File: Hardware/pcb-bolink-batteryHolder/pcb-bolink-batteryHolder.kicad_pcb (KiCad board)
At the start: 2 copper layers, 37 x 64.5 mm, 8 parts, among them J1 Batt-, J2 Batt+, J3 MOLEX PicoBlade 1.25mm

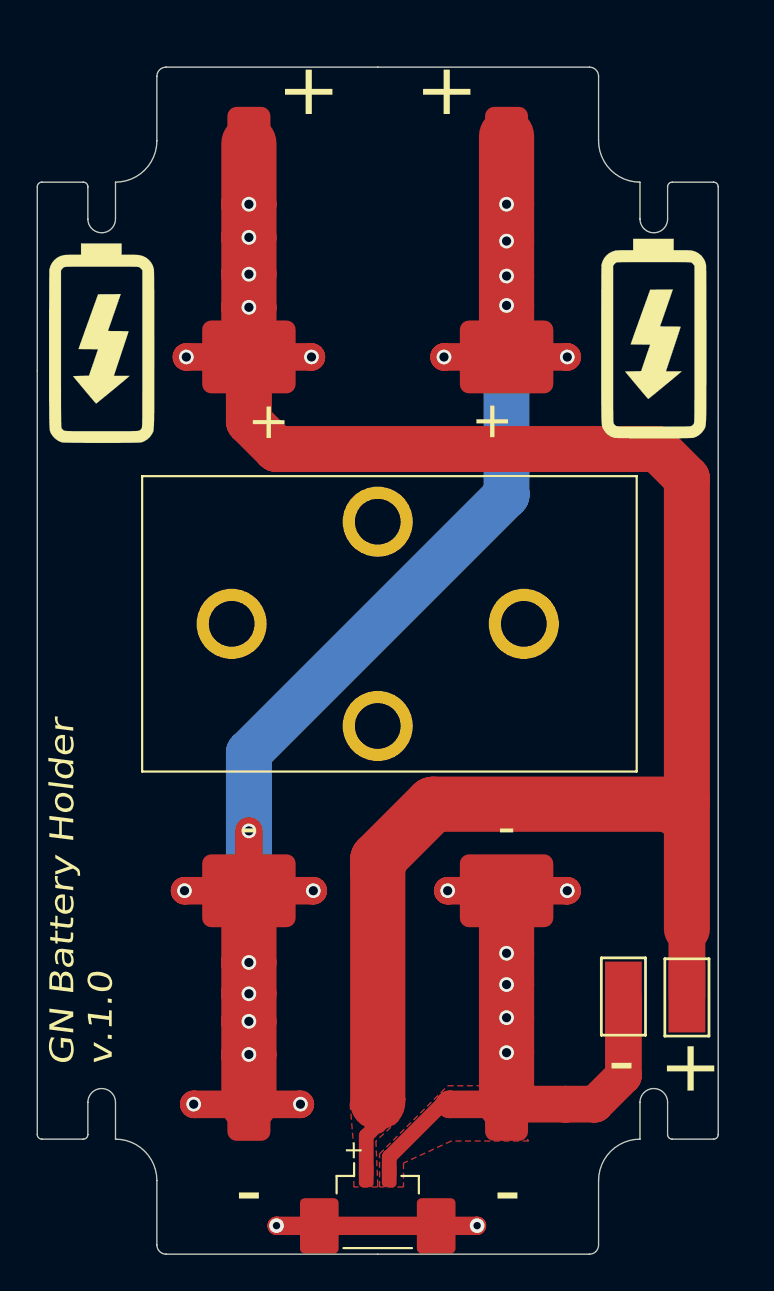
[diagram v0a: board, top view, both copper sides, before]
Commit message: hw: Migrate sch and pcb files to KiCad v6
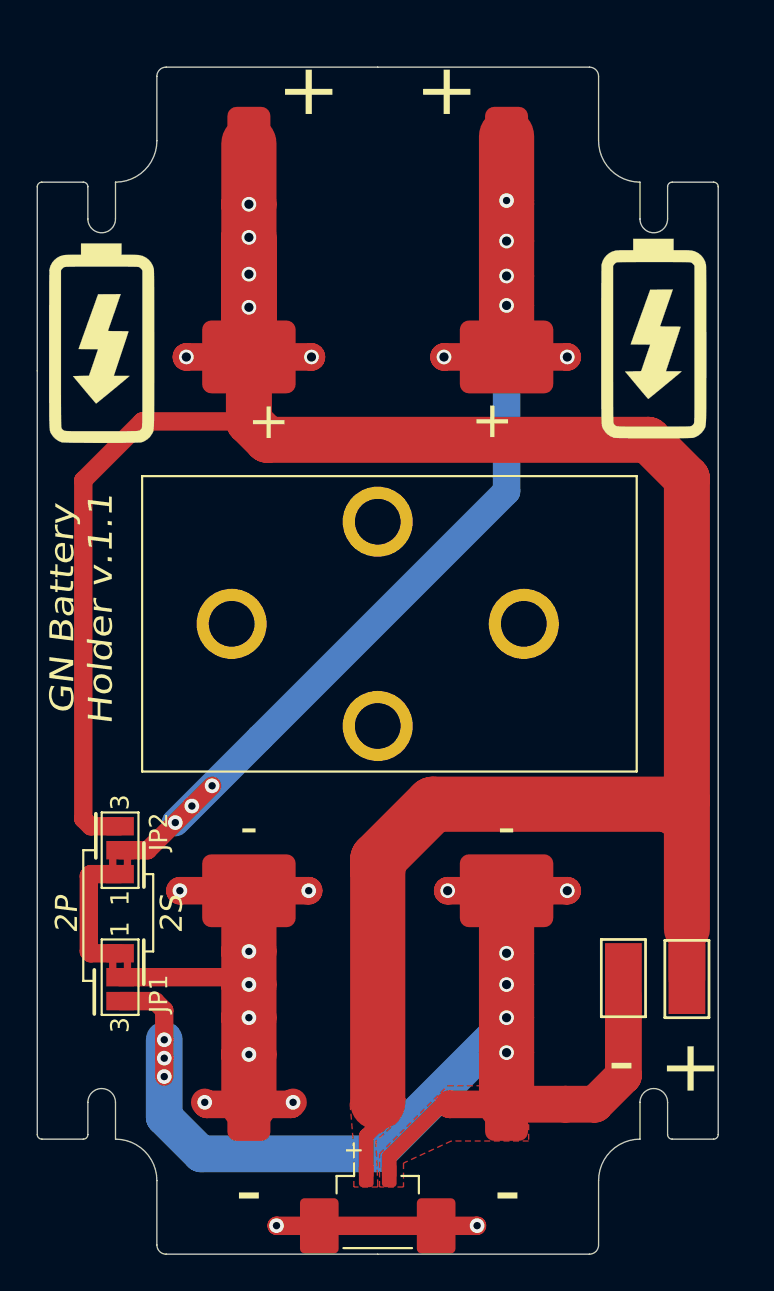
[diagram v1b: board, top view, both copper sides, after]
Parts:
- added JP1: BT2_J, Jumper:SolderJumper-3_P1.3mm_Bridged2Bar12_Pad1.0x1.5mm_NumberLabels, F.Cu at (136.0, 117.2)
- added JP2: BT1_J, Jumper:SolderJumper-3_P1.3mm_Bridged2Bar12_Pad1.0x1.5mm_NumberLabels, F.Cu at (136.0, 110.3)
- BT1, BT2: value 2xPN57 -> PN57
- moved J1 1.00 mm to (163.4, 117.2)
- moved J2 1.00 mm to (166.8, 117.3)
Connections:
- BT2 pad 2: Net-(BT1-Pad1) -> Net-(BT2-Pad2)
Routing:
- net VCC: track 126.3 -> 162.7 mm
- net Net-(BT1-Pad1): track 98.6 -> 64.2 mm, vias 15 -> 9
- net GND: track 41.3 -> 75.5 mm, vias 6 -> 9
- net Net-(BT2-Pad2): track 0.00 -> 30.7 mm, vias 0 -> 8
- net Net-(JP1-Pad1): track 0.00 -> 7.58 mm
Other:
- net class Default removed
- board text added: "2P"
- board text added: "2S"
- board text added: "GN Battery Holder v.1.1"
- board text added: "PN69"
- board text removed: "GN Battery Holder v.1.0"
